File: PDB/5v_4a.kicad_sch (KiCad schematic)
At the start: 13 parts, among them U3 LM76005RNPR

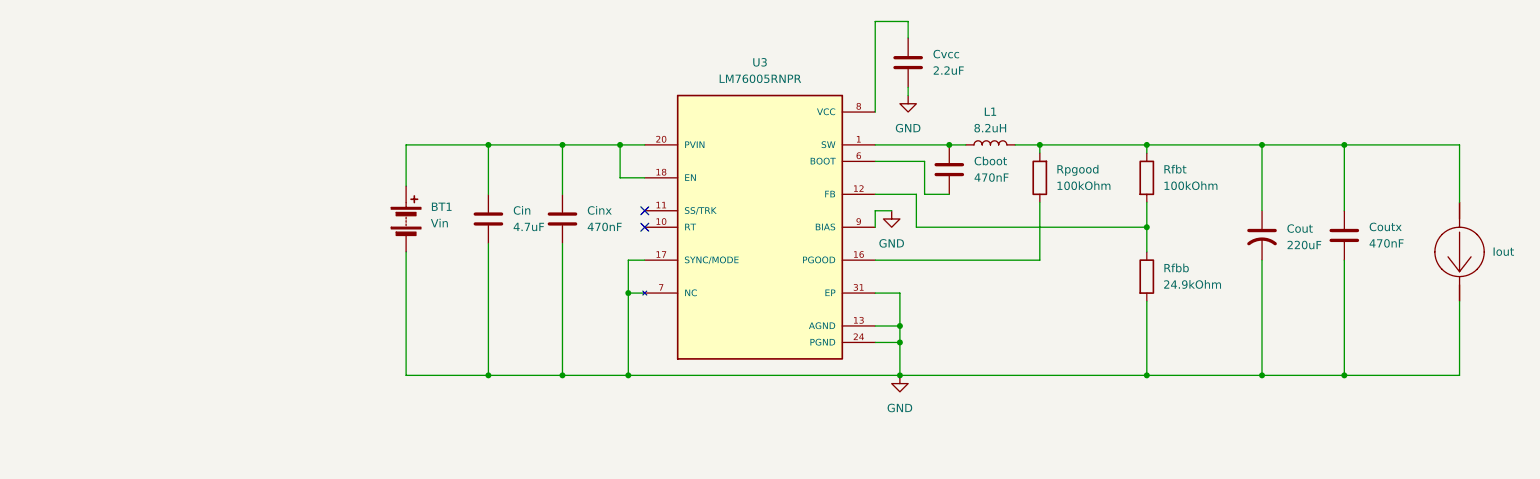
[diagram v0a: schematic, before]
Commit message: Add 3v3@1a
unified the batery lables between sub schematics and changed Iout symbols for power pins to avoid layout issues for trying to match multiple bateries and Iouts without footprints
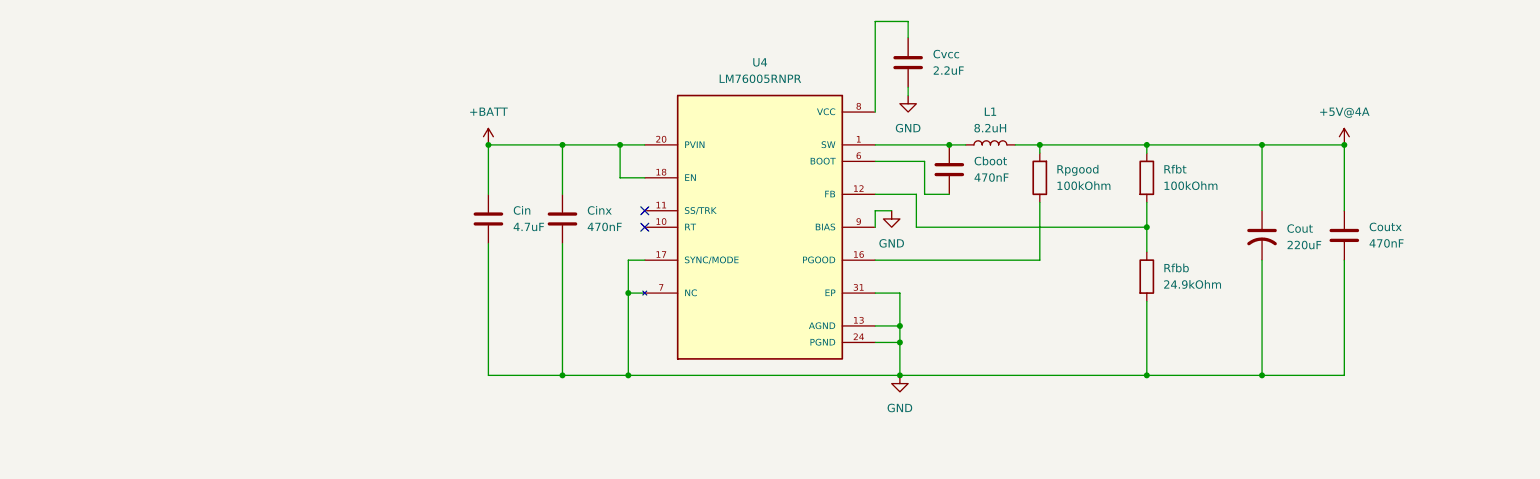
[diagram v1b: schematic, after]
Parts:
- removed BT1: Vin, symbol Device:Battery
- removed Iout: (no value), symbol PDB-altium-import:root_3_Iout_TI WEBENCH
- removed U3: LM76005RNPR, LM76005RNPR:QFN50P600X400X80-31N, symbol LM76005RNPR:LM76005RNPR
- added U4: LM76005RNPR, foot:LM76005RNPR, symbol sym&foot:LM76005RNPR
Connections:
- net AGND: now also U4.13 (AGND), U4.14 (AGND), U4.15 (AGND), U4.17 (SYNC/MODE), U4.19 (NC), U4.23 (NC), U4.24 (PGND), U4.25 (PGND), U4.26 (PGND), U4.27 (NC), U4.28 (NC), U4.29 (NC), U4.30 (NC), U4.31 (EP), U4.7 (NC), U4.9 (BIAS)
- net +BATT: now reaches Cin.1, Cinx.1
- net +BATT: now also U4.18 (EN), U4.20 (PVIN), U4.21 (PVIN), U4.22 (PVIN)
- net +5V@4A: now reaches Cout.1, Coutx.1, L1.2, Rfbt.1, Rpgood.2
- net at Rfbb.1, Rfbt.2: now also U4.12 (FB)
- net at Rpgood.1: now also U4.16 (PGOOD)
- net at Cboot.1, L1.1: now also U4.1 (SW), U4.2 (SW), U4.3 (SW), U4.4 (SW), U4.5 (SW)
- net at Cvcc.1: now also U4.8 (VCC)
- net at Cboot.2: now also U4.6 (BOOT)

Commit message: Add 24V@1.5A
Filled 24V@1.5A schem and added hierarchal pins to each sub sheet
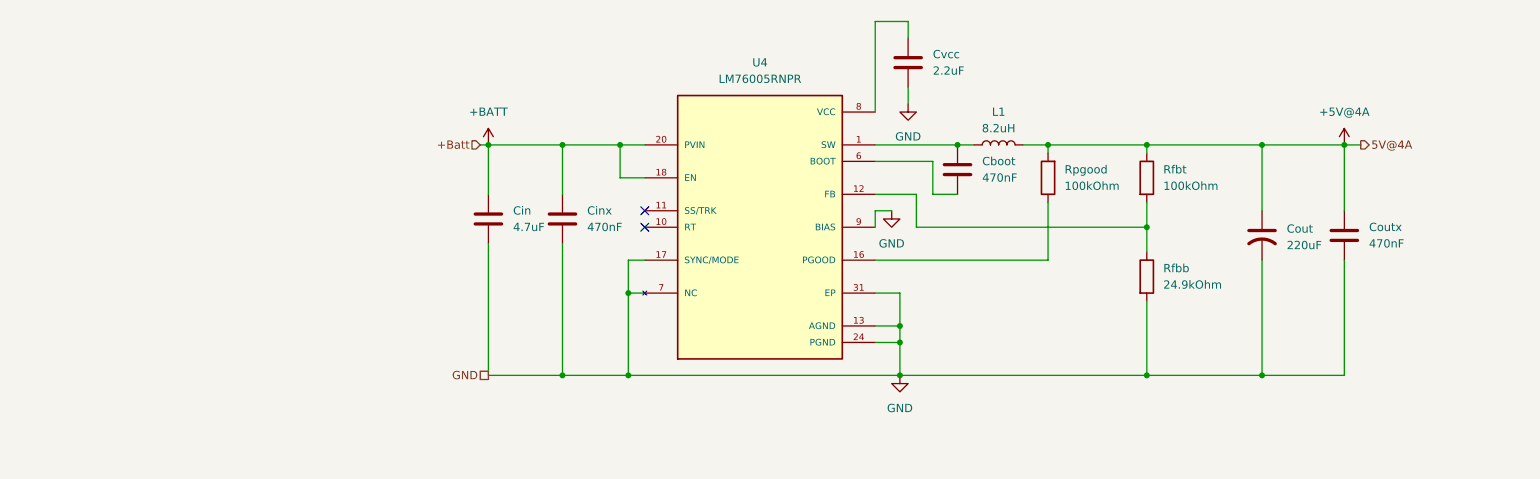
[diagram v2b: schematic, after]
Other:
- moved on the sheet: Cboot, L1, Rpgood
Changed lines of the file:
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@@
 	(paper "A4")
 	(junction
+		(at 201.93 78.74)
+		(diameter 0)
+		(color 0 0 0 0)
+	)
+	(junction
+		(at 111.76 114.3)
+		(diameter 0)
+		(color 0 0 0 0)
+	)
+	(junction
 		(at 201.93 114.3)
 		(diameter 0)
@@
 	)
 	(junction
+		(at 172.72 78.74)
+		(diameter 0)
+		(color 0 0 0 0)
+	)
+	(junction
+		(at 163.83 109.22)
+		(diameter 0)
+		(color 0 0 0 0)
+	)
+	(junction
+		(at 163.83 106.68)
+		(diameter 0)
+		(color 0 0 0 0)
+	)
+	(junction
+		(at 121.92 101.6)
+		(diameter 0)
+		(color 0 0 0 0)
+	)
+	(junction
+		(at 219.71 114.3)
+		(diameter 0)
+		(color 0 0 0 0)
+	)
+	(junction
+		(at 219.71 78.74)
+		(diameter 0)
+		(color 0 0 0 0)
+	)
+	(junction
+		(at 186.69 78.74)
+		(diameter 0)
+		(color 0 0 0 0)
+	)
+	(junction
 		(at 201.93 91.44)
 		(diameter 0)
@@
 	)
 	(junction
-		(at 171.45 78.74)
-		(diameter 0)
-		(color 0 0 0 0)
-	)
-	(junction
-		(at 163.83 109.22)
-		(diameter 0)
-		(color 0 0 0 0)
-	)
-	(junction
-		(at 163.83 106.68)
-		(diameter 0)
-		(color 0 0 0 0)
-	)
-	(junction
-		(at 121.92 101.6)
-		(diameter 0)
-		(color 0 0 0 0)
-	)
-	(junction
-		(at 219.71 114.3)
-		(diameter 0)
-		(color 0 0 0 0)
-	)
-	(junction
-		(at 219.71 78.74)
-		(diameter 0)
-		(color 0 0 0 0)
-	)
-	(junction
-		(at 185.42 78.74)
-		(diameter 0)
-		(color 0 0 0 0)
-	)
-	(junction
-		(at 111.76 114.3)
-		(diameter 0)
-		(color 0 0 0 0)
-	)
-	(junction
 		(at 100.33 78.74)
-		(diameter 0)
-		(color 0 0 0 0)
-	)
-	(junction
-		(at 201.93 78.74)
 		(diameter 0)
 		(color 0 0 0 0)
@@
 	(wire
 		(pts
-			(xy 160.02 81.28) (xy 167.64 81.28)
+			(xy 160.02 81.28) (xy 168.91 81.28)
 		)
 		(stroke
@@
 	(wire
 		(pts
-			(xy 181.61 78.74) (xy 185.42 78.74)
+			(xy 182.88 78.74) (xy 186.69 78.74)
 		)
 		(stroke
@@
 	(wire
 		(pts
+			(xy 121.92 114.3) (xy 163.83 114.3)
+		)
+		(stroke
+			(width 0)
+			(type default)
+		)
+	)
+	(wire
+		(pts
 			(xy 163.83 114.3) (xy 201.93 114.3)
 		)
@@
 	(wire
 		(pts
+			(xy 99.06 78.74) (xy 100.33 78.74)
+		)
+		(stroke
+			(width 0)
+			(type default)
+		)
+	)
+	(wire
+		(pts
 			(xy 160.02 88.9) (xy 162.56 88.9)
 		)
@@
 	(wire
 		(pts
-			(xy 165.1 69.85) (xy 165.1 71.12)
+			(xy 165.1 69.85) (xy 165.1 72.39)
 		)
 		(stroke
@@
 	(wire
 		(pts
-			(xy 121.92 114.3) (xy 163.83 114.3)
-		)
-		(stroke
-			(width 0)
-			(type default)
-		)
-	)
-	(wire
-		(pts
 			(xy 160.02 86.36) (xy 166.37 86.36)
 		)
@@
 	(wire
 		(pts
-			(xy 185.42 96.52) (xy 160.02 96.52)
+			(xy 186.69 96.52) (xy 160.02 96.52)
 		)
 		(stroke
@@
 	(wire
 		(pts
-			(xy 167.64 86.36) (xy 171.45 86.36)
+			(xy 168.91 86.36) (xy 172.72 86.36)
+		)
+		(stroke
+			(width 0)
+			(type default)
+		)
+	)
+	(wire
+		(pts
+			(xy 232.41 78.74) (xy 234.95 78.74)
 		)
 		(stroke
@@
 	(wire
 		(pts
-			(xy 167.64 81.28) (xy 167.64 86.36)
+			(xy 168.91 81.28) (xy 168.91 86.36)
 		)
 		(stroke
@@
 	(wire
 		(pts
-			(xy 160.02 78.74) (xy 171.45 78.74)
-		)
-		(stroke
-			(width 0)
-			(type default)
-		)
-	)
-	(wire
-		(pts
-			(xy 185.42 78.74) (xy 201.93 78.74)
-		)
-		(stroke
-			(width 0)
-			(type default)
-		)
-	)
-	(wire
-		(pts
-			(xy 185.42 78.74) (xy 185.42 80.01)
+			(xy 160.02 78.74) (xy 172.72 78.74)
+		)
+		(stroke
+			(width 0)
+			(type default)
+		)
+	)
+	(wire
+		(pts
+			(xy 186.69 78.74) (xy 201.93 78.74)
+		)
+		(stroke
+			(width 0)
+			(type default)
+		)
+	)
+	(wire
+		(pts
+			(xy 186.69 78.74) (xy 186.69 80.01)
 		)
 		(stroke
@@
 	(wire
 		(pts
-			(xy 185.42 87.63) (xy 185.42 96.52)
+			(xy 186.69 87.63) (xy 186.69 96.52)
 		)
 		(stroke
@@
 	(wire
 		(pts
-			(xy 171.45 78.74) (xy 173.99 78.74)
-		)
-		(stroke
-			(width 0)
-			(type default)
+			(xy 172.72 78.74) (xy 175.26 78.74)
+		)
+		(stroke
+			(width 0)
+			(type default)
+		)
+	)
+	(hierarchical_label "GND"
+		(shape passive)
+		(at 100.33 114.3 180)
+		(effects
+			(font
+				(size 1.27 1.27)
+			)
+			(justify right)
+		)
+	)
+	(hierarchical_label "+Batt"
+		(shape input)
+		(at 99.06 78.74 180)
+		(effects
+			(font
+				(size 1.27 1.27)
+			)
+			(justify right)
+		)
+	)
+	(hierarchical_label "5V@4A"
+		(shape output)
+		(at 234.95 78.74 0)
+		(effects
+			(font
+				(size 1.27 1.27)
+			)
+			(justify left)
 		)
 	)
@@
 	(symbol
 		(lib_id "Device:R")
-		(at 185.42 83.82 180)
+		(at 186.69 83.82 180)
 		(unit 1)
 		(body_style 1)
@@
 		(fields_autoplaced yes)
 		(property "Reference" "Rpgood"
-			(at 187.96 82.5499 0)
+			(at 189.23 82.5499 0)
 			(show_name no)
 			(do_not_autoplace no)
@@
 		)
 		(property "Value" "100kOhm"
-			(at 187.96 85.0899 0)
+			(at 189.23 85.0899 0)
 			(show_name no)
 			(do_not_autoplace no)
@@
 		)
 		(property "Footprint" ""
-			(at 187.198 83.82 90)
+			(at 188.468 83.82 90)
 			(hide yes)
 			(show_name no)
@@
 		)
 		(property "Datasheet" ""
-			(at 185.42 83.82 0)
+			(at 186.69 83.82 0)
 			(hide yes)
 			(show_name no)
@@
 		)
 		(property "Description" "Resistor"
-			(at 185.42 83.82 0)
+			(at 186.69 83.82 0)
 			(hide yes)
 			(show_name no)
@@
 	(symbol
 		(lib_id "Device:L")
-		(at 177.8 78.74 90)
+		(at 179.07 78.74 90)
 		(unit 1)
 		(body_style 1)
@@
 		(fields_autoplaced yes)
 		(property "Reference" "L1"
-			(at 177.8 73.66 90)
+			(at 179.07 73.66 90)
 			(show_name no)
 			(do_not_autoplace no)
@@
 		)
 		(property "Value" "8.2uH"
-			(at 177.8 76.2 90)
+			(at 179.07 76.2 90)
 			(show_name no)
 			(do_not_autoplace no)
@@
 		)
 		(property "Footprint" ""
-			(at 177.8 78.74 0)
+			(at 179.07 78.74 0)
 			(hide yes)
 			(show_name no)
@@
 		)
 		(property "Datasheet" ""
-			(at 177.8 78.74 0)
+			(at 179.07 78.74 0)
 			(hide yes)
 			(show_name no)
@@
 		)
 		(property "Description" "Inductor"
-			(at 177.8 78.74 0)
+			(at 179.07 78.74 0)
 			(hide yes)
 			(show_name no)
@@
 	(symbol
 		(lib_id "power:GND")
-		(at 165.1 71.12 0)
+		(at 165.1 72.39 0)
 		(unit 1)
 		(body_style 1)
@@
 		(fields_autoplaced yes)
 		(property "Reference" "#PWR03"
+			(at 165.1 78.74 0)
+			(hide yes)
+			(show_name no)
+			(do_not_autoplace no)
+			(effects
+				(font
+					(size 1.27 1.27)
+				)
+			)
+		)
+		(property "Value" "GND"
 			(at 165.1 77.47 0)
-			(hide yes)
-			(show_name no)
-			(do_not_autoplace no)
-			(effects
-				(font
-					(size 1.27 1.27)
-				)
-			)
-		)
-		(property "Value" "GND"
-			(at 165.1 76.2 0)
 			(show_name no)
 			(do_not_autoplace no)
@@
 		)
 		(property "Footprint" ""
-			(at 165.1 71.12 0)
+			(at 165.1 72.39 0)
 			(hide yes)
 			(show_name no)
@@
 		)
 		(property "Datasheet" ""
-			(at 165.1 71.12 0)
+			(at 165.1 72.39 0)
 			(hide yes)
 			(show_name no)
@@
 		)
 		(property "Description" "Power symbol creates a global label with name \"GND\" , ground"
-			(at 165.1 71.12 0)
+			(at 165.1 72.39 0)
 			(hide yes)
 			(show_name no)
@@
 	(symbol
 		(lib_id "Device:C")
-		(at 171.45 82.55 0)
+		(at 172.72 82.55 0)
 		(unit 1)
 		(body_style 1)
@@
 		(fields_autoplaced yes)
 		(property "Reference" "Cboot"
-			(at 175.26 81.2799 0)
+			(at 176.53 81.2799 0)
 			(show_name no)
 			(do_not_autoplace no)
@@
 		)
 		(property "Value" "470nF"
-			(at 175.26 83.8199 0)
+			(at 176.53 83.8199 0)
 			(show_name no)
 			(do_not_autoplace no)
@@
 		)
 		(property "Footprint" ""
-			(at 172.4152 86.36 0)
+			(at 173.6852 86.36 0)
 			(hide yes)
 			(show_name no)
@@
 		)
 		(property "Datasheet" ""
-			(at 171.45 82.55 0)
+			(at 172.72 82.55 0)
 			(hide yes)
 			(show_name no)
@@
 		)
 		(property "Description" "Unpolarized capacitor"
-			(at 171.45 82.55 0)
-			(hide yes)
-			(show_name no)
+			(at 172.72 82.55 0)
+			(hide yes)
+			(show_name no)

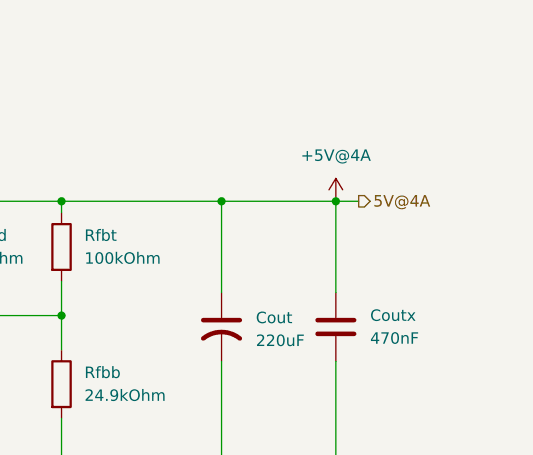
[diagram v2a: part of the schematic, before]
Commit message: added fuses to each
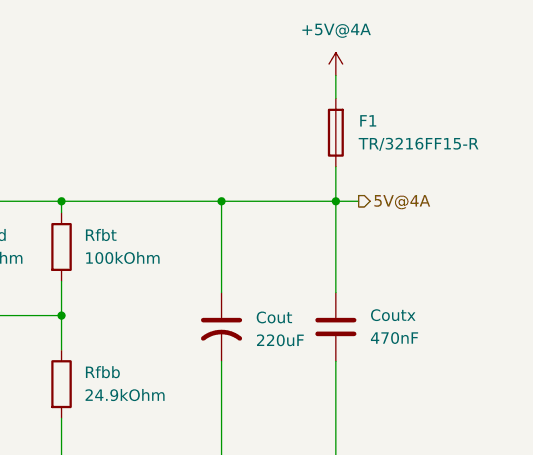
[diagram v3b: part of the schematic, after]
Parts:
- added F1: TR/3216FF15-R, symbol Device:Fuse
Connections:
- net +5V@4A: now also F1.2; no longer Cout.1, Coutx.1, L1.2, Rfbt.1, Rpgood.2
- new net 5V@4A: Cout.1, Coutx.1, F1.1, L1.2, Rfbt.1, Rpgood.2
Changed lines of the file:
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@@
 	(wire
 		(pts
-			(xy 232.41 78.74) (xy 232.41 88.9)
+			(xy 232.41 74.93) (xy 232.41 88.9)
 		)
 		(stroke
@@
 		(pts
 			(xy 120.65 78.74) (xy 124.46 78.74)
+		)
+		(stroke
+			(width 0)
+			(type default)
+		)
+	)
+	(wire
+		(pts
+			(xy 232.41 64.77) (xy 232.41 67.31)
 		)
 		(stroke
@@
 	)
 	(symbol
+		(lib_id "Device:Fuse")
+		(at 232.41 71.12 180)
+		(unit 1)
+		(body_style 1)
+		(exclude_from_sim no)
+		(in_bom yes)
+		(on_board yes)
+		(in_pos_files yes)
+		(dnp no)
+		(fields_autoplaced yes)
+		(property "Reference" "F1"
+			(at 234.95 69.8499 0)
+			(show_name no)
+			(do_not_autoplace no)
+			(effects
+				(font
+					(size 1.27 1.27)
+				)
+				(justify right)
+			)
+		)
+		(property "Value" "TR/3216FF15-R"
+			(at 234.95 72.3899 0)
+			(show_name no)
+			(do_not_autoplace no)
+			(effects
+				(font
+					(size 1.27 1.27)
+				)
+				(justify right)
+			)
+		)
+		(property "Footprint" ""
+			(at 234.188 71.12 90)
+			(hide yes)
+			(show_name no)
+			(do_not_autoplace no)
+			(effects
+				(font
+					(size 1.27 1.27)
+				)
+			)
+		)
+		(property "Datasheet" ""
+			(at 232.41 71.12 0)
+			(hide yes)
+			(show_name no)
+			(do_not_autoplace no)
+			(effects
+				(font
+					(size 1.27 1.27)
+				)
+			)
+		)
+		(property "Description" "Fuse"
+			(at 232.41 71.12 0)
+			(hide yes)
+			(show_name no)
+			(do_not_autoplace no)
+			(effects
+				(font
+					(size 1.27 1.27)
+				)
+			)
+		)
+		(pin "2"
+		)
+		(pin "1"
+		)
+		(instances
+			(project "PDB"
+				(path "/a9cf05c4-aac5-4cf1-b700-1d3045f8dfbd/fb4943bd-b408-4249-996b-df676f2bb727"
+					(reference "F1")
+					(unit 1)
+				)
+			)
+		)
+	)
+	(symbol
 		(lib_id "Device:C_US")
 		(at 219.71 92.71 0)
@@
 	(symbol
 		(lib_id "power:+1V5")
-		(at 232.41 78.74 0)
+		(at 232.41 64.77 0)
 		(unit 1)
 		(body_style 1)
@@
 		(fields_autoplaced yes)
 		(property "Reference" "#PWR010"
-			(at 232.41 82.55 0)
+			(at 232.41 68.58 0)
 			(hide yes)
 			(show_name no)
@@
 		)
 		(property "Value" "+5V@4A"
-			(at 232.41 73.66 0)
+			(at 232.41 59.69 0)
 			(show_name no)
 			(do_not_autoplace no)
@@
 		)
 		(property "Footprint" ""
-			(at 232.41 78.74 0)
+			(at 232.41 64.77 0)
 			(hide yes)
 			(show_name no)
@@
 		)
 		(property "Datasheet" ""
-			(at 232.41 78.74 0)
+			(at 232.41 64.77 0)
 			(hide yes)
 			(show_name no)
@@
 		)
 		(property "Description" "Power symbol creates a global label with name \"+1V5\""
-			(at 232.41 78.74 0)
-			(hide yes)
-			(show_name no)
+			(at 232.41 64.77 0)
+			(hide yes)
+			(show_name no)

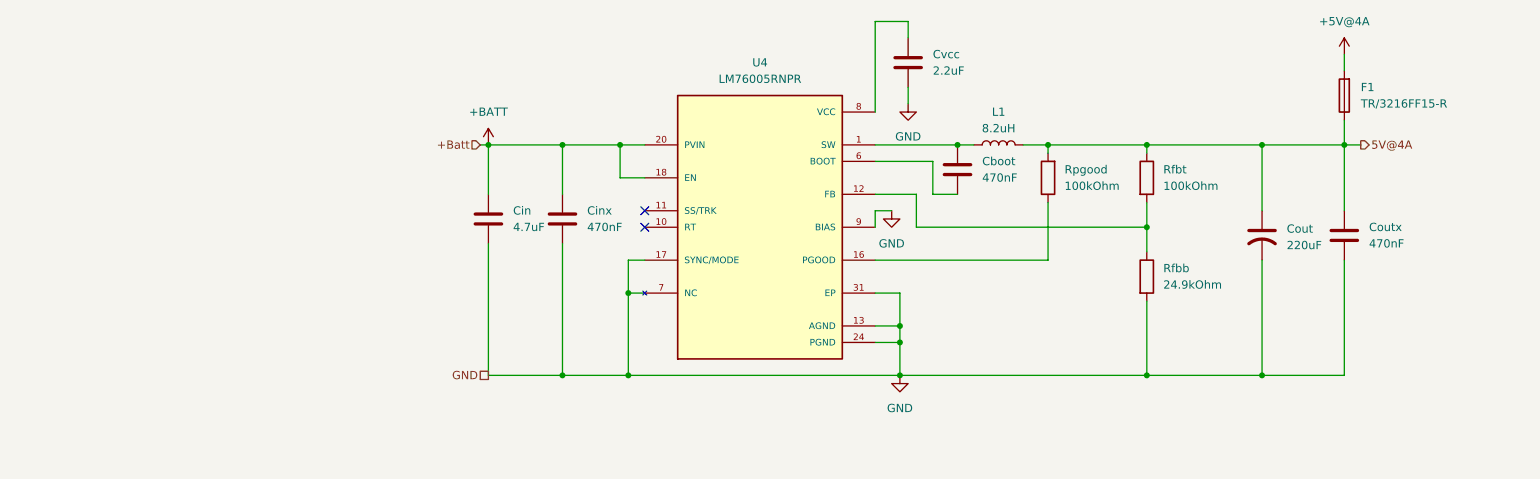
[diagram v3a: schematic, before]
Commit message: added temp sensing on every rail available
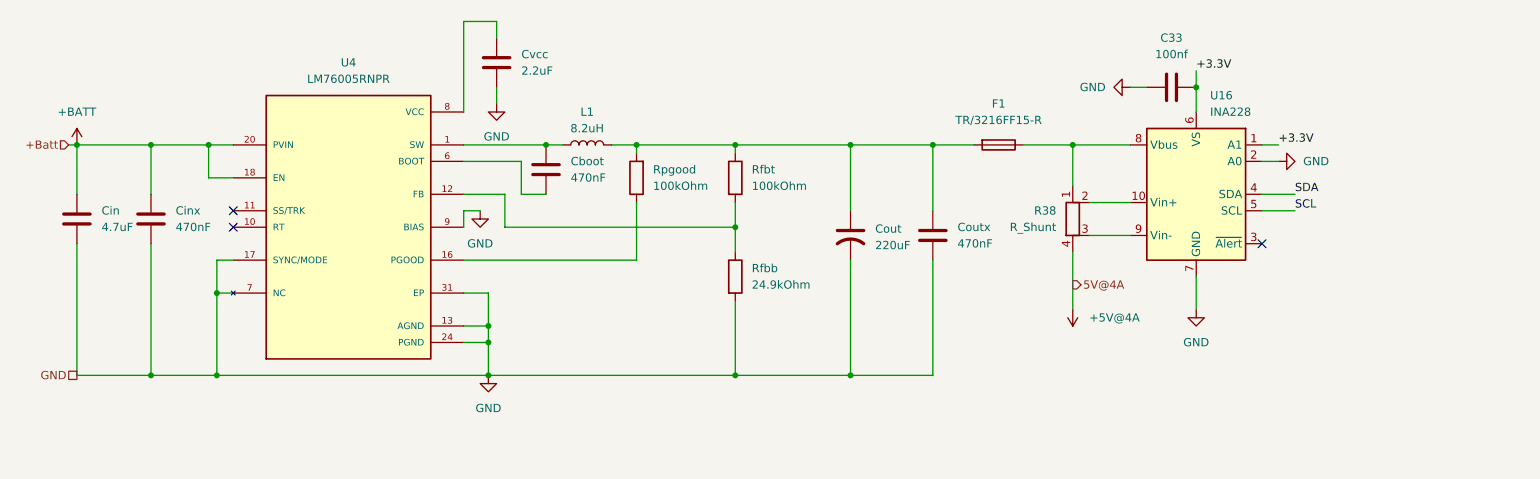
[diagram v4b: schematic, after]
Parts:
- added C33: 100nf, Capacitor_SMD:C_1206_3216Metric, symbol Device:C
- added R38: R_Shunt, symbol Device:R_Shunt
- added U16: INA228, Package_SO:TSSOP-10_3x3mm_P0.5mm, symbol Sensor_Energy:INA228
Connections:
- net +5V@4A: now also R38.4; no longer F1.2
- net AGND: now also C33.1, U16.2 (A0), U16.7 (GND)
- net 5V@4A: no longer names the net of Cout.1, Coutx.1, L1.2, Rfbt.1, Rpgood.2
- net 5V@4A: now also F1.2; no longer F1.1
- new net: F1.1, R38.1, U16.8 (Vbus)
- new net: R38.2, U16.10 (Vin+)
- new net: R38.3, U16.9 (Vin-)
- new net +3.3V: C33.2, U16.1 (A1), U16.6 (VS)
- new net SCL: U16.5 (SCL)
- new net SDA: U16.4 (SDA)
- no-connect marks 2 -> 3
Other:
- moved on the sheet: Cboot, Cin, Cinx, Cout, Coutx, Cvcc, F1, L1, Rfbb, Rfbt, Rpgood, U4
